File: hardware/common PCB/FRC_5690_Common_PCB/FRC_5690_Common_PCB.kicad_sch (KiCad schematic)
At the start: 40 parts, among them J1 5V in, J10 UART, J11 LED 0, J12 LED 1, J13 Analog In, J14 Micro_SD_Card, J17 Conn_01x03_Pin, J18 Conn_01x03_Pin, J19 Conn_01x03_Pin, J2 I2C 0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

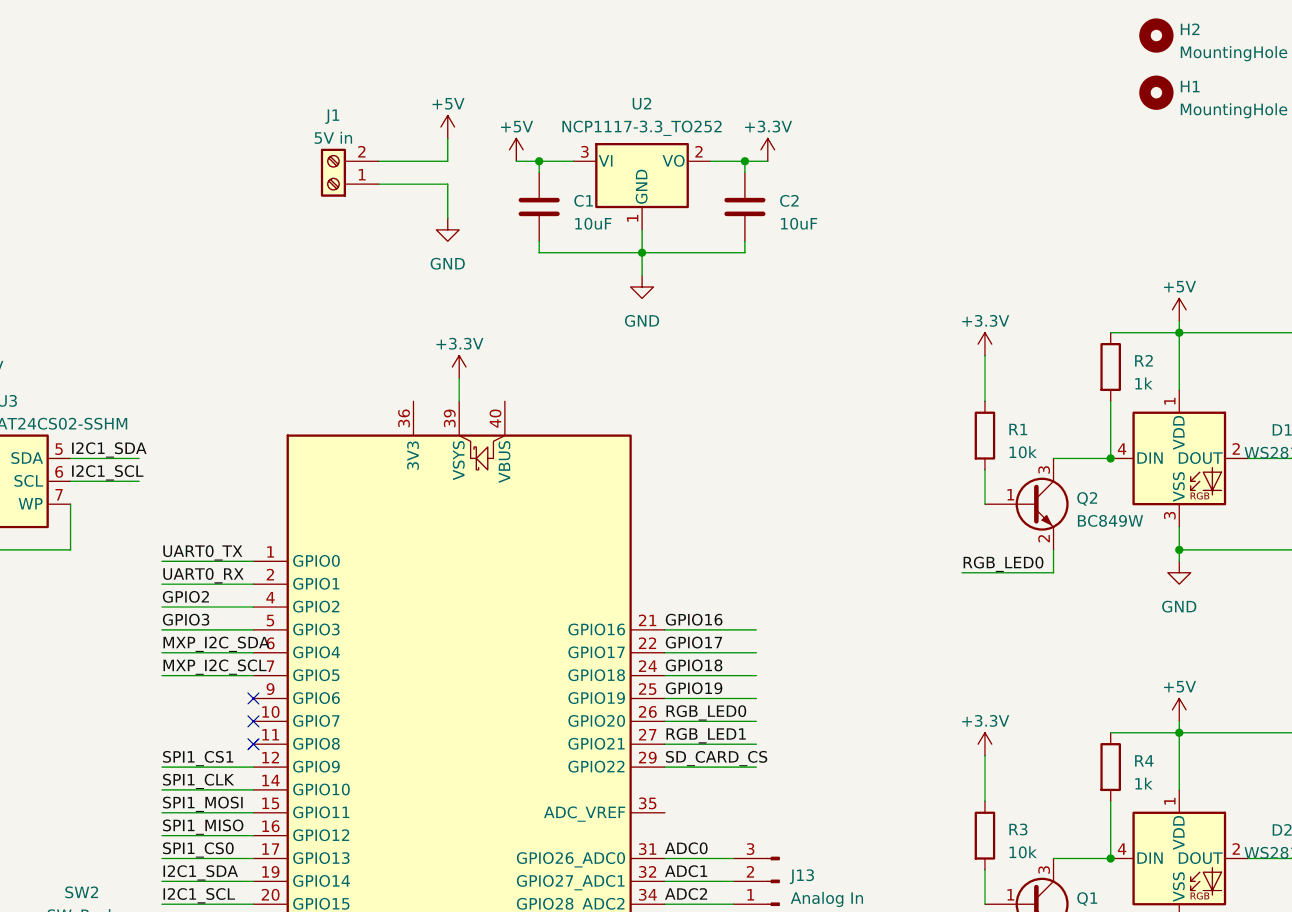
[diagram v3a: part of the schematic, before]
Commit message: add commands for controlling board
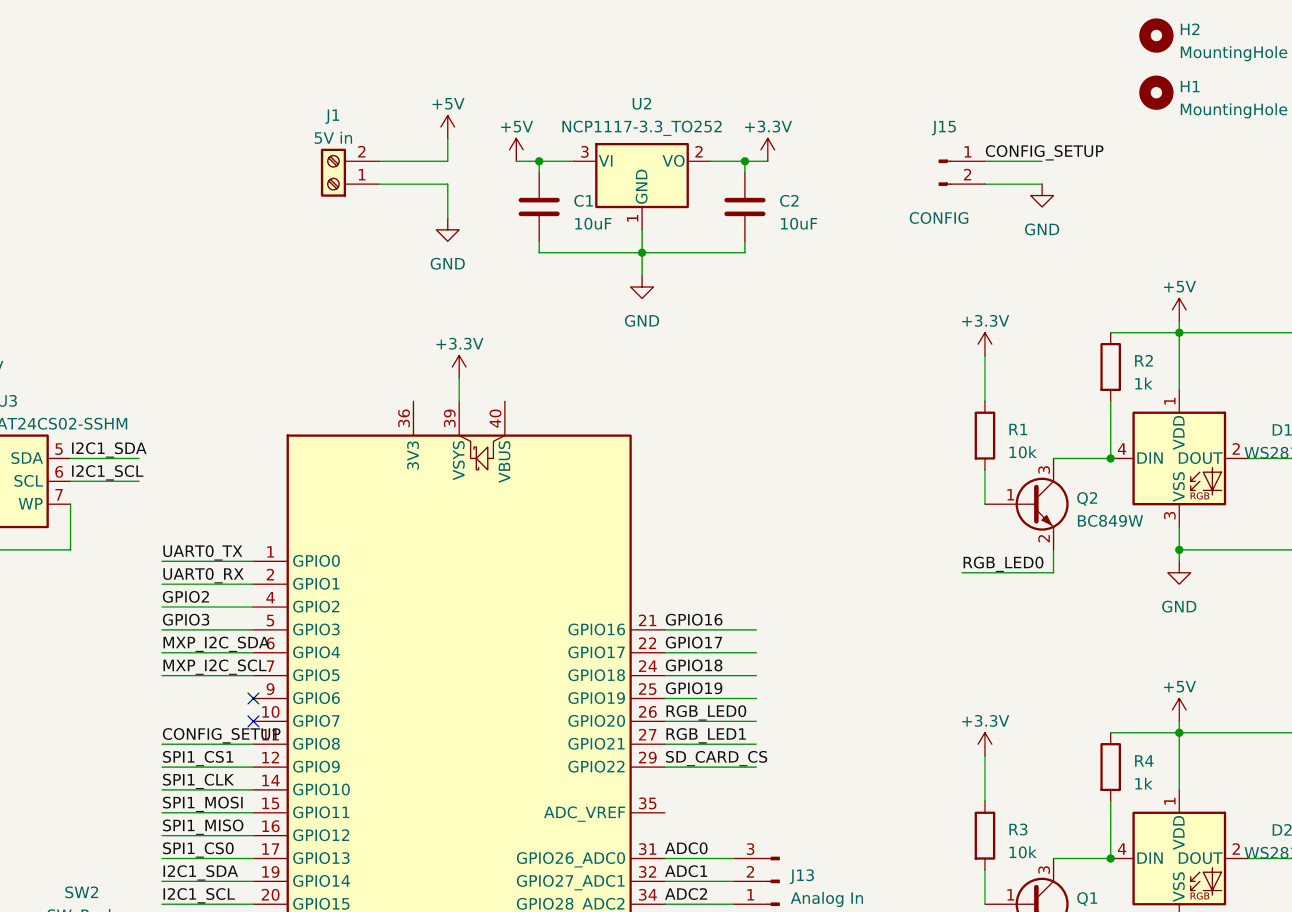
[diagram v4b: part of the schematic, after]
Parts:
- added J15: CONFIG, Connector_PinHeader_2.54mm:PinHeader_1x02_P2.54mm_Vertical, symbol Connector:Conn_01x02_Pin
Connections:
- net GND: now also J15.2 (Pin_2)
- net CONFIG_SETUP: now reaches U1.11 (GPIO8)
- net CONFIG_SETUP: now also J15.1 (Pin_1)
- no-connect marks 5 -> 4
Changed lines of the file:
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@@
   (no_connect (at 236.22 137.16))
   (no_connect (at 129.54 92.71))
-  (no_connect (at 129.54 95.25))
   (no_connect (at 129.54 90.17))
   (wire (pts (xy 210.82 96.52) (xy 210.82 101.6))
@@
     (stroke (width 0) (type default))
   )
+  (wire (pts (xy 210.82 33.02) (xy 217.17 33.02))
+    (stroke (width 0) (type default))
+  )
   (wire (pts (xy 40.64 43.18) (xy 46.99 43.18))
     (stroke (width 0) (type default))
@@
     (stroke (width 0) (type default))
   )
+  (wire (pts (xy 119.38 95.25) (xy 129.54 95.25))
+    (stroke (width 0) (type default))
+  )
   (wire (pts (xy 232.41 115.57) (xy 232.41 118.11))
     (stroke (width 0) (type default))
@@
     (stroke (width 0) (type default))
   )
+  (wire (pts (xy 210.82 30.48) (xy 217.17 30.48))
+    (stroke (width 0) (type default))
+  )
   (wire (pts (xy 224.79 93.98) (xy 232.41 93.98))
     (stroke (width 0) (type default))
@@
     (effects (font (size 1.27 1.27)) (justify left bottom))
   )
+  (label "CONFIG_SETUP" (at 119.38 95.25 0) (fields_autoplaced)
+    (effects (font (size 1.27 1.27)) (justify left bottom))
+  )
   (label "MXP_AI2" (at 36.83 152.4 0) (fields_autoplaced)
     (effects (font (size 1.27 1.27)) (justify left bottom))
@@
     (effects (font (size 1.27 1.27)) (justify left bottom))
   )
+  (label "CONFIG_SETUP" (at 210.82 30.48 0) (fields_autoplaced)
+    (effects (font (size 1.27 1.27)) (justify left bottom))
+  )
   (label "SPI1_CLK" (at 41.91 73.66 0) (fields_autoplaced)
     (effects (font (size 1.27 1.27)) (justify left bottom))
@@
     )
   )
+  (symbol (lib_id "Connector:Conn_01x02_Pin") (at 205.74 30.48 0) (unit 1)
+    (in_bom yes) (on_board yes) (dnp no)
+    (property "Reference" "J15" (at 206.375 26.67 0)
+      (effects (font (size 1.27 1.27)))
+    )
+    (property "Value" "CONFIG" (at 205.74 36.83 0)
+      (effects (font (size 1.27 1.27)))
+    )
+    (property "Footprint" "Connector_PinHeader_2.54mm:PinHeader_1x02_P2.54mm_Vertical" (at 205.74 30.48 0)
+      (effects (font (size 1.27 1.27)) hide)
+    )
+    (property "Datasheet" "~" (at 205.74 30.48 0)
+      (effects (font (size 1.27 1.27)) hide)
+    )
+    (pin "1")
+    (pin "2")
+    (instances
+      (project "FRC_5690_Common_PCB"
+        (path "/61912a13-ede8-48b1-a32d-9390036060d9"
+          (reference "J15") (unit 1)
+        )
+      )
+    )
+  )
   (symbol (lib_id "Connector:Conn_01x03_Pin") (at 196.85 146.05 0) (unit 1)
     (in_bom yes) (on_board yes) (dnp no) (fields_autoplaced)
@@
         )
       )
+    )
+  )
+  (symbol (lib_id "power:GND") (at 217.17 33.02 0) (unit 1)
+    (in_bom yes) (on_board yes) (dnp no) (fields_autoplaced)
+    (property "Reference" "#PWR033" (at 217.17 39.37 0)
+      (effects (font (size 1.27 1.27)) hide)
+    )
+    (property "Value" "GND" (at 217.17 38.1 0)
+      (effects (font (size 1.27 1.27)))
+    )
+    (property "Footprint" "" (at 217.17 33.02 0)
+      (effects (font (size 1.27 1.27)) hide)
+    )
+    (property "Datasheet" "" (at 217.17 33.02 0)
+      (effects (font (size 1.27 1.27)) hide)
+    )
+    (pin "1")
+    (instances
+      (project "FRC_5690_Common_PCB"
+        (path "/61912a13-ede8-48b1-a32d-9390036060d9"
+          (reference "#PWR033") (unit 1)
+        )
+      )
